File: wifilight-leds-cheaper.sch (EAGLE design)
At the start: 51 parts, among them J2 CON_HEADER_PRG_AVR_ICSP-PTH, Q1 BUK98180-100A, Q2 BUK98180-100A, Q3 BUK98180-100A, Q4 BUK98180-100A, U2 PCA9685

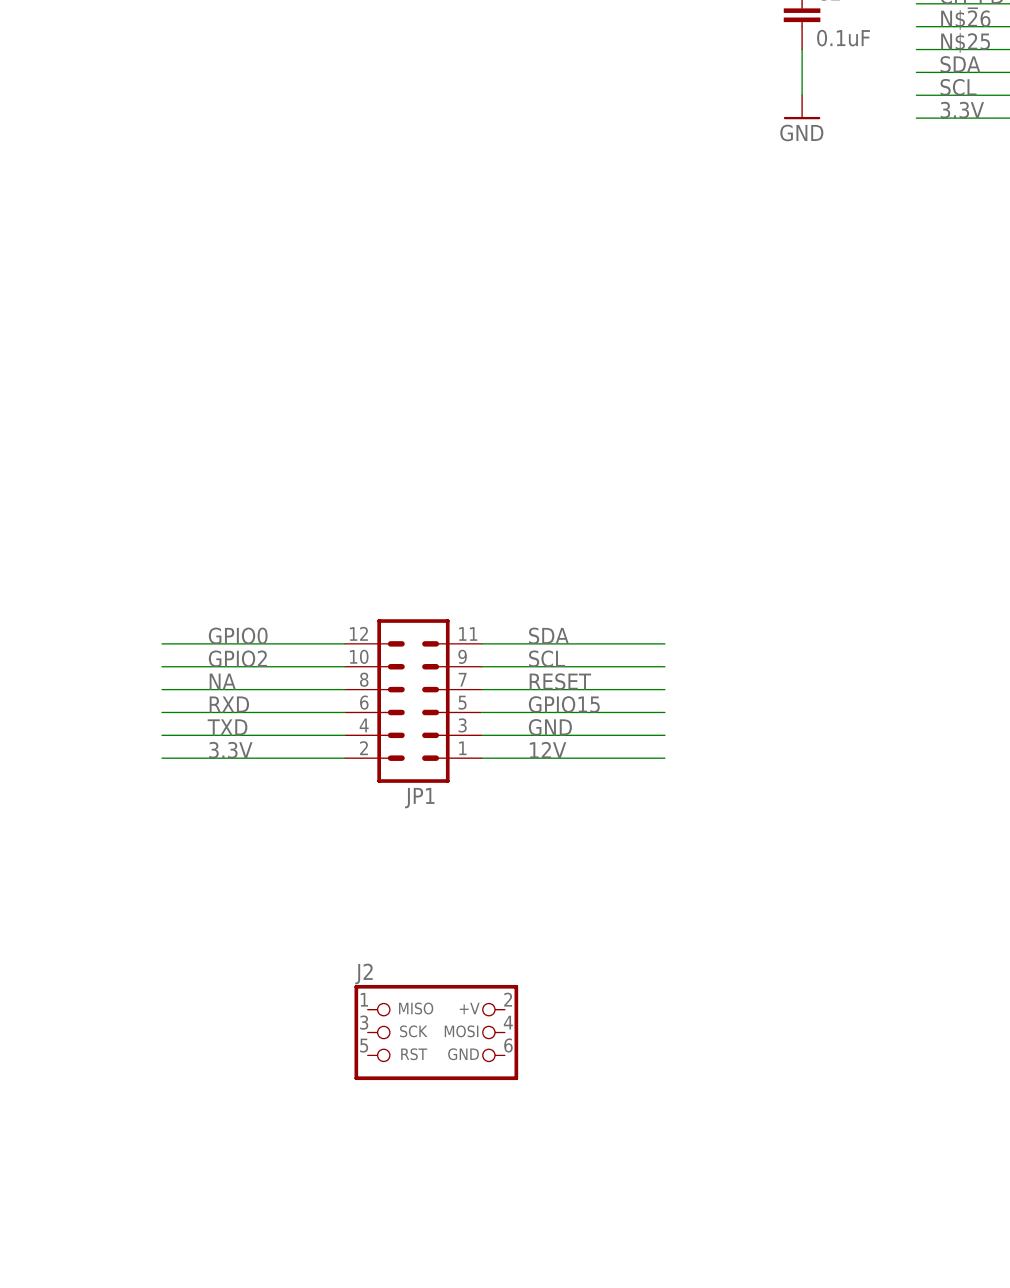
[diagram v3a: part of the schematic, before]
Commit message: Added 3x4 pin headers. Added 2x i2c JST connectors.
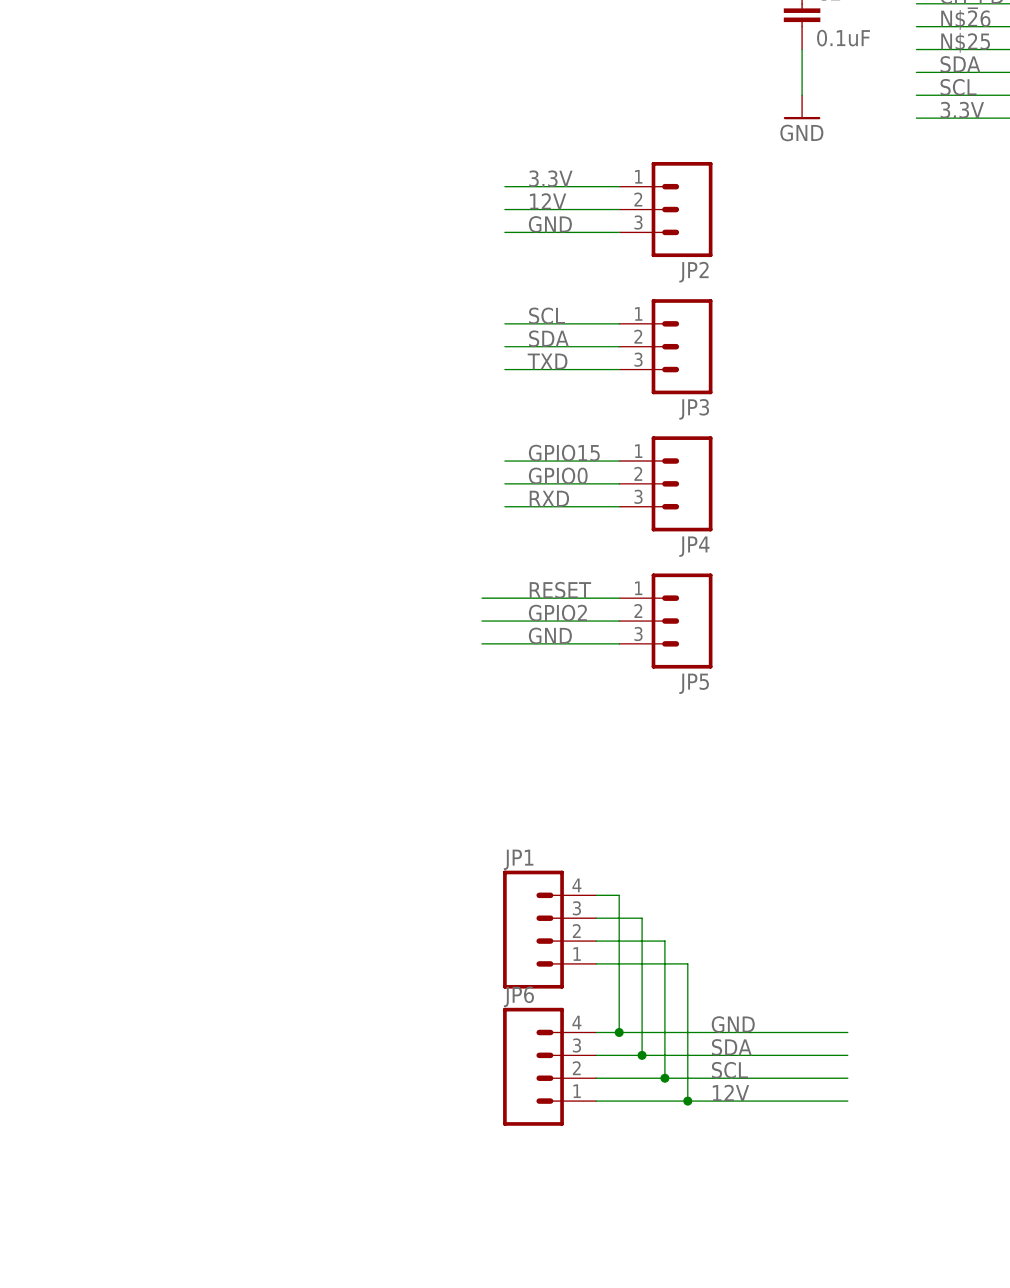
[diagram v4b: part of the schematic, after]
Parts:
- removed J2: CON_HEADER_PRG_AVR_ICSP-PTH, dp_devices:CON_HEADER_PRG_AVR_ICSP-PTH
- added JP2, JP3, JP4, JP5: (no value), SparkFun-Connectors:M03LOCK_NO_SILK
- added JP6: (no value), SparkFun-Connectors:M04JST
- JP1: device SparkFun-Connectors:M06X2FEMALE-SMT -> SparkFun-Connectors:M04JST
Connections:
- removed net NA: JP1.8
- net 12V: now also JP2.2, JP6.1
- net 3.3V: now also JP2.1; no longer JP1.2
- net GND: now also JP1.4, JP2.3, JP5.3, JP6.4; no longer JP1.3
- net GPIO0: now also JP4.2; no longer JP1.12
- net GPIO15: now also JP4.1; no longer JP1.5
- net GPIO2: now also JP5.2; no longer JP1.10
- net RESET: now also JP5.1; no longer JP1.7
- net RXD: now also JP4.3; no longer JP1.6
- net SCL: now also JP1.2, JP3.1, JP6.2; no longer JP1.9
- net SDA: now also JP1.3, JP3.2, JP6.3; no longer JP1.11
- net TXD: now also JP3.3; no longer JP1.4
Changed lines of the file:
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@@
 <part name="SUPPLY2" library="SparkFun-Aesthetics" deviceset="12V" device=""/>
 <part name="GND7" library="SparkFun-Aesthetics" deviceset="GND" device=""/>
-<part name="JP1" library="SparkFun-Connectors" deviceset="M06X2" device="FEMALE-SMT"/>
-<part name="J2" library="dp_devices" deviceset="CON_HEADER_PRG_AVR_ICSP" device="-PTH"/>
+<part name="JP2" library="SparkFun-Connectors" deviceset="M03" device="LOCK_NO_SILK"/>
+<part name="JP3" library="SparkFun-Connectors" deviceset="M03" device="LOCK_NO_SILK"/>
+<part name="JP4" library="SparkFun-Connectors" deviceset="M03" device="LOCK_NO_SILK"/>
+<part name="JP5" library="SparkFun-Connectors" deviceset="M03" device="LOCK_NO_SILK"/>
+<part name="JP1" library="SparkFun-Connectors" deviceset="M04" device="JST"/>
+<part name="JP6" library="SparkFun-Connectors" deviceset="M04" device="JST"/>
 </parts>
 <sheets>
@@
 <instance part="SUPPLY2" gate="G$1" x="-83.82" y="165.1"/>
 <instance part="GND7" gate="1" x="-83.82" y="144.78"/>
-<instance part="JP1" gate="G$1" x="20.32" y="-7.62" rot="R180"/>
-<instance part="J2" gate="J" x="20.32" y="-50.8"/>
+<instance part="JP2" gate="G$1" x="48.26" y="40.64" rot="R180"/>
+<instance part="JP3" gate="G$1" x="48.26" y="25.4" rot="R180"/>
+<instance part="JP4" gate="G$1" x="48.26" y="10.16" rot="R180"/>
+<instance part="JP5" gate="G$1" x="48.26" y="-5.08" rot="R180"/>
+<instance part="JP1" gate="G$1" x="33.02" y="-40.64"/>
+<instance part="JP6" gate="G$1" x="33.02" y="-55.88"/>
 </instances>
 <busses>
@@
 </segment>
 <segment>
-<wire x1="45.72" y1="-17.78" x2="25.4" y2="-17.78" width="0.1524" layer="91"/>
-<label x="30.48" y="-17.78" size="1.778" layer="95"/>
-<pinref part="JP1" gate="G$1" pin="3"/>
+<pinref part="JP2" gate="G$1" pin="3"/>
+<wire x1="40.64" y1="38.1" x2="27.94" y2="38.1" width="0.1524" layer="91"/>
+<label x="30.48" y="38.1" size="1.778" layer="95"/>
+</segment>
+<segment>
+<pinref part="JP5" gate="G$1" pin="3"/>
+<wire x1="40.64" y1="-7.62" x2="25.4" y2="-7.62" width="0.1524" layer="91"/>
+<label x="30.48" y="-7.62" size="1.778" layer="95"/>
+</segment>
+<segment>
+<pinref part="JP6" gate="G$1" pin="4"/>
+<wire x1="38.1" y1="-50.8" x2="40.64" y2="-50.8" width="0.1524" layer="91"/>
+<wire x1="40.64" y1="-50.8" x2="40.64" y2="-35.56" width="0.1524" layer="91"/>
+<pinref part="JP1" gate="G$1" pin="4"/>
+<wire x1="40.64" y1="-35.56" x2="38.1" y2="-35.56" width="0.1524" layer="91"/>
+<wire x1="66.04" y1="-50.8" x2="40.64" y2="-50.8" width="0.1524" layer="91"/>
+<junction x="40.64" y="-50.8"/>
+<label x="50.8" y="-50.8" size="1.778" layer="95"/>
 </segment>
 </net>
@@
 </segment>
 <segment>
-<wire x1="45.72" y1="-10.16" x2="25.4" y2="-10.16" width="0.1524" layer="91"/>
-<label x="30.48" y="-10.16" size="1.778" layer="95"/>
-<pinref part="JP1" gate="G$1" pin="9"/>
+<pinref part="JP3" gate="G$1" pin="1"/>
+<wire x1="27.94" y1="27.94" x2="40.64" y2="27.94" width="0.1524" layer="91"/>
+<label x="30.48" y="27.94" size="1.778" layer="95"/>
+</segment>
+<segment>
+<pinref part="JP1" gate="G$1" pin="2"/>
+<wire x1="38.1" y1="-40.64" x2="45.72" y2="-40.64" width="0.1524" layer="91"/>
+<wire x1="45.72" y1="-40.64" x2="45.72" y2="-55.88" width="0.1524" layer="91"/>
+<pinref part="JP6" gate="G$1" pin="2"/>
+<wire x1="45.72" y1="-55.88" x2="38.1" y2="-55.88" width="0.1524" layer="91"/>
+<wire x1="66.04" y1="-55.88" x2="45.72" y2="-55.88" width="0.1524" layer="91"/>
+<junction x="45.72" y="-55.88"/>
+<label x="50.8" y="-55.88" size="1.778" layer="95"/>
 </segment>
 </net>
@@
 </segment>
 <segment>
-<wire x1="25.4" y1="-7.62" x2="45.72" y2="-7.62" width="0.1524" layer="91"/>
-<label x="30.48" y="-7.62" size="1.778" layer="95"/>
-<pinref part="JP1" gate="G$1" pin="11"/>
+<pinref part="JP3" gate="G$1" pin="2"/>
+<wire x1="40.64" y1="25.4" x2="27.94" y2="25.4" width="0.1524" layer="91"/>
+<label x="30.48" y="25.4" size="1.778" layer="95"/>
+</segment>
+<segment>
+<pinref part="JP1" gate="G$1" pin="3"/>
+<wire x1="38.1" y1="-38.1" x2="43.18" y2="-38.1" width="0.1524" layer="91"/>
+<wire x1="43.18" y1="-38.1" x2="43.18" y2="-53.34" width="0.1524" layer="91"/>
+<pinref part="JP6" gate="G$1" pin="3"/>
+<wire x1="43.18" y1="-53.34" x2="38.1" y2="-53.34" width="0.1524" layer="91"/>
+<wire x1="43.18" y1="-53.34" x2="66.04" y2="-53.34" width="0.1524" layer="91"/>
+<junction x="43.18" y="-53.34"/>
+<label x="50.8" y="-53.34" size="1.778" layer="95"/>
 </segment>
 </net>
@@
 </segment>
 <segment>
-<wire x1="45.72" y1="-20.32" x2="25.4" y2="-20.32" width="0.1524" layer="91"/>
-<label x="30.48" y="-20.32" size="1.778" layer="95"/>
-<pinref part="JP1" gate="G$1" pin="1"/>
-</segment>
-<segment>
 <pinref part="C3" gate="G$1" pin="+"/>
 <wire x1="-83.82" y1="160.02" x2="-83.82" y2="165.1" width="0.1524" layer="91"/>
 <pinref part="SUPPLY2" gate="G$1" pin="12V"/>
+</segment>
+<segment>
+<pinref part="JP2" gate="G$1" pin="2"/>
+<wire x1="27.94" y1="40.64" x2="40.64" y2="40.64" width="0.1524" layer="91"/>
+<label x="30.48" y="40.64" size="1.778" layer="95"/>
+</segment>
+<segment>
+<pinref part="JP6" gate="G$1" pin="1"/>
+<wire x1="38.1" y1="-58.42" x2="48.26" y2="-58.42" width="0.1524" layer="91"/>
+<wire x1="48.26" y1="-58.42" x2="48.26" y2="-43.18" width="0.1524" layer="91"/>
+<pinref part="JP1" gate="G$1" pin="1"/>
+<wire x1="48.26" y1="-43.18" x2="38.1" y2="-43.18" width="0.1524" layer="91"/>
+<wire x1="48.26" y1="-58.42" x2="66.04" y2="-58.42" width="0.1524" layer="91"/>
+<junction x="48.26" y="-58.42"/>
+<label x="50.8" y="-58.42" size="1.778" layer="95"/>
 </segment>
 </net>
@@
 </segment>
 <segment>
-<wire x1="-10.16" y1="-20.32" x2="10.16" y2="-20.32" width="0.1524" layer="91"/>
-<label x="-5.08" y="-20.32" size="1.778" layer="95"/>
-<pinref part="JP1" gate="G$1" pin="2"/>
+<pinref part="JP2" gate="G$1" pin="1"/>
+<wire x1="40.64" y1="43.18" x2="27.94" y2="43.18" width="0.1524" layer="91"/>
+<label x="30.48" y="43.18" size="1.778" layer="95"/>
 </segment>
 </net>
@@
 </segment>
 <segment>
-<wire x1="25.4" y1="-12.7" x2="45.72" y2="-12.7" width="0.1524" layer="91"/>
-<label x="30.48" y="-12.7" size="1.778" layer="95"/>
-<pinref part="JP1" gate="G$1" pin="7"/>
+<pinref part="JP5" gate="G$1" pin="1"/>
+<wire x1="40.64" y1="-2.54" x2="25.4" y2="-2.54" width="0.1524" layer="91"/>
+<label x="30.48" y="-2.54" size="1.778" layer="95"/>
 </segment>
 </net>
@@
 </segment>
 <segment>
-<wire x1="10.16" y1="-7.62" x2="-10.16" y2="-7.62" width="0.1524" layer="91"/>
-<label x="-5.08" y="-7.62" size="1.778" layer="95"/>
-<pinref part="JP1" gate="G$1" pin="12"/>
+<pinref part="JP4" gate="G$1" pin="2"/>
+<wire x1="40.64" y1="10.16" x2="27.94" y2="10.16" width="0.1524" layer="91"/>
+<label x="30.48" y="10.16" size="1.778" layer="95"/>
 </segment>
 </net>
@@
 </segment>
 <segment>
-<wire x1="-10.16" y1="-10.16" x2="10.16" y2="-10.16" width="0.1524" layer="91"/>
-<label x="-5.08" y="-10.16" size="1.778" layer="95"/>
-<pinref part="JP1" gate="G$1" pin="10"/>
+<pinref part="JP5" gate="G$1" pin="2"/>
+<wire x1="25.4" y1="-5.08" x2="40.64" y2="-5.08" width="0.1524" layer="91"/>
+<label x="30.48" y="-5.08" size="1.778" layer="95"/>
 </segment>
 </net>
@@
 </segment>
 <segment>
-<pinref part="JP1" gate="G$1" pin="4"/>
-<wire x1="10.16" y1="-17.78" x2="-10.16" y2="-17.78" width="0.1524" layer="91"/>
-<label x="-5.08" y="-17.78" size="1.778" layer="95"/>
+<pinref part="JP3" gate="G$1" pin="3"/>
+<wire x1="40.64" y1="22.86" x2="27.94" y2="22.86" width="0.1524" layer="91"/>
+<label x="30.48" y="22.86" size="1.778" layer="95"/>
 </segment>
 </net>
@@
 </segment>
 <segment>
-<wire x1="-10.16" y1="-15.24" x2="10.16" y2="-15.24" width="0.1524" layer="91"/>
-<label x="-5.08" y="-15.24" size="1.778" layer="95"/>
-<pinref part="JP1" gate="G$1" pin="6"/>
+<pinref part="JP4" gate="G$1" pin="3"/>
+<wire x1="27.94" y1="7.62" x2="40.64" y2="7.62" width="0.1524" layer="91"/>
+<label x="30.48" y="7.62" size="1.778" layer="95"/>
 </segment>
 </net>
@@
 </segment>
 <segment>
-<wire x1="45.72" y1="-15.24" x2="25.4" y2="-15.24" width="0.1524" layer="91"/>
-<label x="30.48" y="-15.24" size="1.778" layer="95"/>
-<pinref part="JP1" gate="G$1" pin="5"/>
-</segment>
-</net>
-<net name="NA" class="0">
-<segment>
-<wire x1="10.16" y1="-12.7" x2="-10.16" y2="-12.7" width="0.1524" layer="91"/>
-<label x="-5.08" y="-12.7" size="1.778" layer="95"/>
-<pinref part="JP1" gate="G$1" pin="8"/>
-</segment>
-</net>
+<pinref part="JP4" gate="G$1" pin="1"/>
+<wire x1="27.94" y1="12.7" x2="40.64" y2="12.7" width="0.1524" layer="91"/>
+<label x="30.48" y="12.7" size="1.778" layer="95"/>
+</segment>
+</net>

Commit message: Mk6 complete & DRC'd
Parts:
- removed A, B: (no value), adafruit:PINHD-1X1
- removed JP1, JP6: (no value), SparkFun-Connectors:M04JST
- removed JP2, JP3, JP4, JP5: (no value), SparkFun-Connectors:M03LOCK_NO_SILK
- removed LB1, LB2, LB3, LG1, LG2, LG3, LR1, LR2, LR3: XPEWHT-01-0000-00BC2, led:XPEWHT-01-0000-00BC2
- removed P_RED, P_WHITE, RED, SCL, SDA, TP12V, TP3.3V, TPCHPD, TPGND, TPGPIO0, TPGPIO2, TPRX, TPTX, WHITE: TEST-POINT3X5, SparkFun-Passives:TEST-POINT3X5
- removed U2: PCA9685, adafruit:PCA9685
- added CN1: (no value), adafruit:JST_2PIN-THM
- added LED1, LED2, LED3, LED4, LED5, LED6: RGBLED5050, adafruit:RGBLED5050
- added R10, R11, R12, R13: 10k, SparkFun-Resistors:RESISTOR1206
- added U1: TCA6507PW, Texas Instruments_By_element14_Batch_1:TCA6507PW
- added X1: 53261-06, con-molex:53261-06
- C1, C2, C6, C7: device resistor:C-EUC0805K -> SparkFun-Passives:CAP1206
- R2, R7: value ??? -> 220ohm; device resistor:R-EU_R0805 -> SparkFun-Passives:RESISTOR1206
- R5, R6, R8: device resistor:R-EU_R0805 -> SparkFun-Passives:RESISTOR1206
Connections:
- net N$25 renamed GPIO14
- net N$26 renamed GPIO16
- net N$28 renamed ADC
- removed net #OE: R8.2, U2.#OE
- removed net B1: LB2.A, LB3.C
- removed net B2: LB1.A, LB2.C
- removed net G1: LG2.A, LG3.C
- removed net G2: LG1.A, LG2.C
- removed net N$18: A.1, B2.AC1
- removed net N$19: B.1, B2.AC2
- removed net N$36: MPU.GPIO5
- removed net R1: LR2.A, LR3.C
- removed net R2: LR1.A, LR2.C
- new net AC1: B2.AC1, CN1.2
- new net AC2: B2.AC2, CN1.1
- new net EN: R8.2, U1.EN
- new net GPIO12: MPU.GPIO12
- new net GPIO13: MPU.GPIO13
- new net N$30: LED2.RED_C, LED3.RED_A
- new net N$31: LED2.GREEN_C, LED3.GREEN_A
- new net N$32: LED2.BLUE_C, LED3.BLUE_A
- new net N$33: LED1.RED_C, LED2.RED_A
- new net N$34: LED1.GREEN_C, LED2.GREEN_A
- new net N$35: LED1.BLUE_C, LED2.BLUE_A
- new net N$37: LED4.RED_C, LED5.RED_A
- new net N$38: LED4.GREEN_C, LED5.GREEN_A
- new net N$39: LED4.BLUE_C, LED5.BLUE_A
- new net N$40: LED5.RED_C, LED6.RED_A
- new net N$41: LED5.GREEN_C, LED6.GREEN_A
- new net N$42: LED5.BLUE_C, LED6.BLUE_A
- new net N$6: U1.P2
- new net POWERED: R2.1, U1.P0
- net 12V: now also LED1.BLUE_A, LED1.GREEN_A, LED1.RED_A, LED4.BLUE_A, LED4.GREEN_A, LED4.RED_A, X1-6.S; no longer JP1.1, JP2.2, JP6.1, LB3.A, LG3.A, LR3.A, TP12V.1
- net 3.3V: now also R10.1, R11.1, R12.1, R8.1, U1.VCC; no longer JP2.1, R2.1, TP3.3V.1, U2.VDD
- net BLUE: now also U1.P4; no longer U2.PWM0
- net CH_PD: now also R11.2; no longer TPCHPD.1
- net GND: now also R13.1, U1.GND, U1.NC, U1.NC_2, X1-5.S; no longer JP1.4, JP2.3, JP5.3, JP6.4, R8.1, TPGND.1, U2.EXTCLK, U2.GND
- net GPIO0: now also R12.2, X1-4.S; no longer JP4.2, TPGPIO0.1
- net GPIO15: now also R13.2; no longer JP4.1
- net GPIO2: no longer JP5.2, TPGPIO2.1
- net GREEN: now also U1.P6; no longer U2.PWM1
- net P_BLUE: now also LED3.BLUE_C, LED6.BLUE_C; no longer LB1.C
- net P_GREEN: now also LED3.GREEN_C, LED6.GREEN_C; no longer LG1.C
- net P_RED: now also LED3.RED_C, LED6.RED_C; no longer LR1.C, P_RED.1
- net P_WHITE: no longer P_WHITE.1
- net RED: now also U1.P5; no longer RED.1, U2.PWM2
- net RESET: now also R10.2, X1-3.S; no longer JP5.1
- net RXD: now also X1-2.S; no longer JP4.3, TPRX.1
- net SCL: now also MPU.GPIO5, U1.SCL; no longer JP1.2, JP3.1, JP6.2, MPU.GPIO13, SCL.1, U2.SCL
- net SDA: now also MPU.GPIO4, U1.SDA; no longer JP1.3, JP3.2, JP6.3, MPU.GPIO12, SDA.1, U2.SDA
- net THINKING: now also U1.P1; no longer MPU.GPIO4
- net TXD: now also X1-1.S; no longer JP3.3, TPTX.1
- net WHITE: now also U1.P3; no longer U2.PWM3, WHITE.1
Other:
- moved on the sheet: C1, C2, C6, C7
